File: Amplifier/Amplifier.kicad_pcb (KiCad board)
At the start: 4 copper layers, 94 x 58.4 mm, 47 parts, among them J1 132365-10, J2 SMA-J-P-H-ST-EM1, J3 JST_VH, U1 SKY65111-348LF, U2 MAX2633EUT+T, U3 RLM-23-1WL+, U4 SKYA21001, U5 SKYA21001, U6 TPS63051RMWR

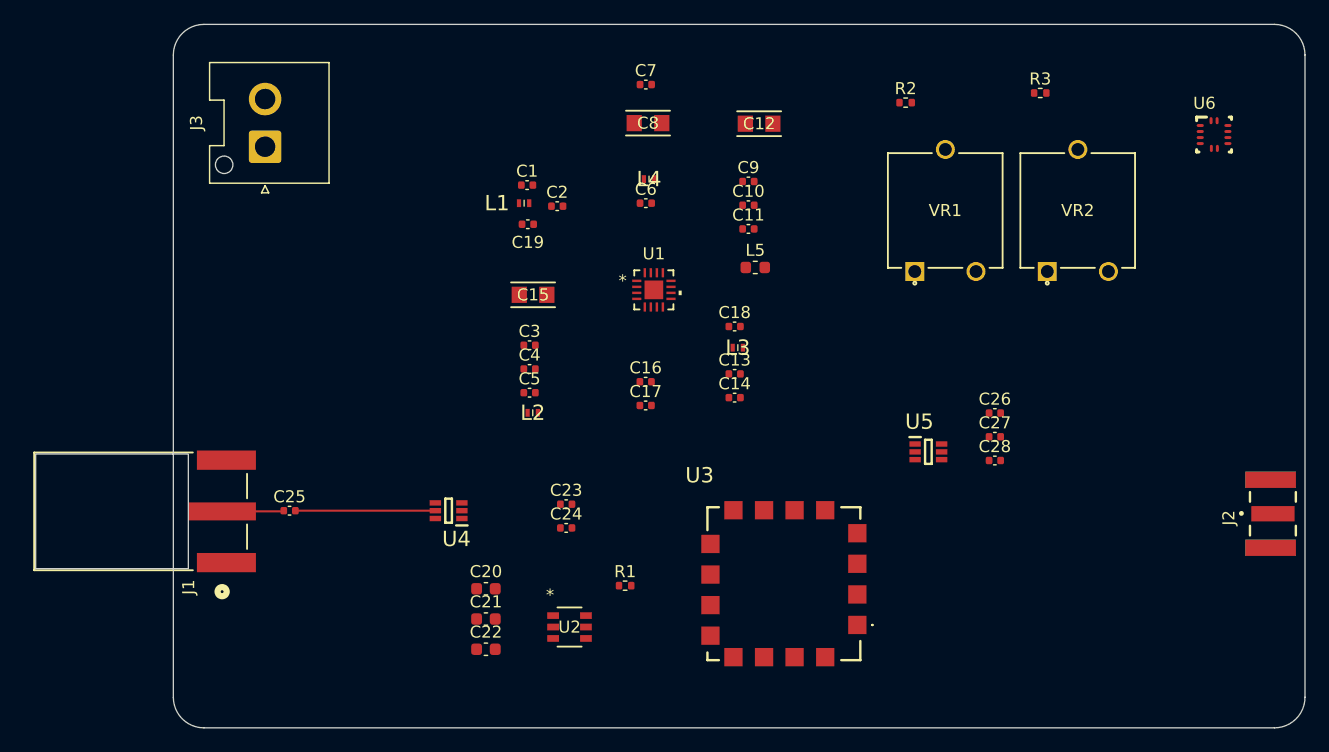
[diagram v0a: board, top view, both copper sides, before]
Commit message: updated component footprint. updated pcb layout.
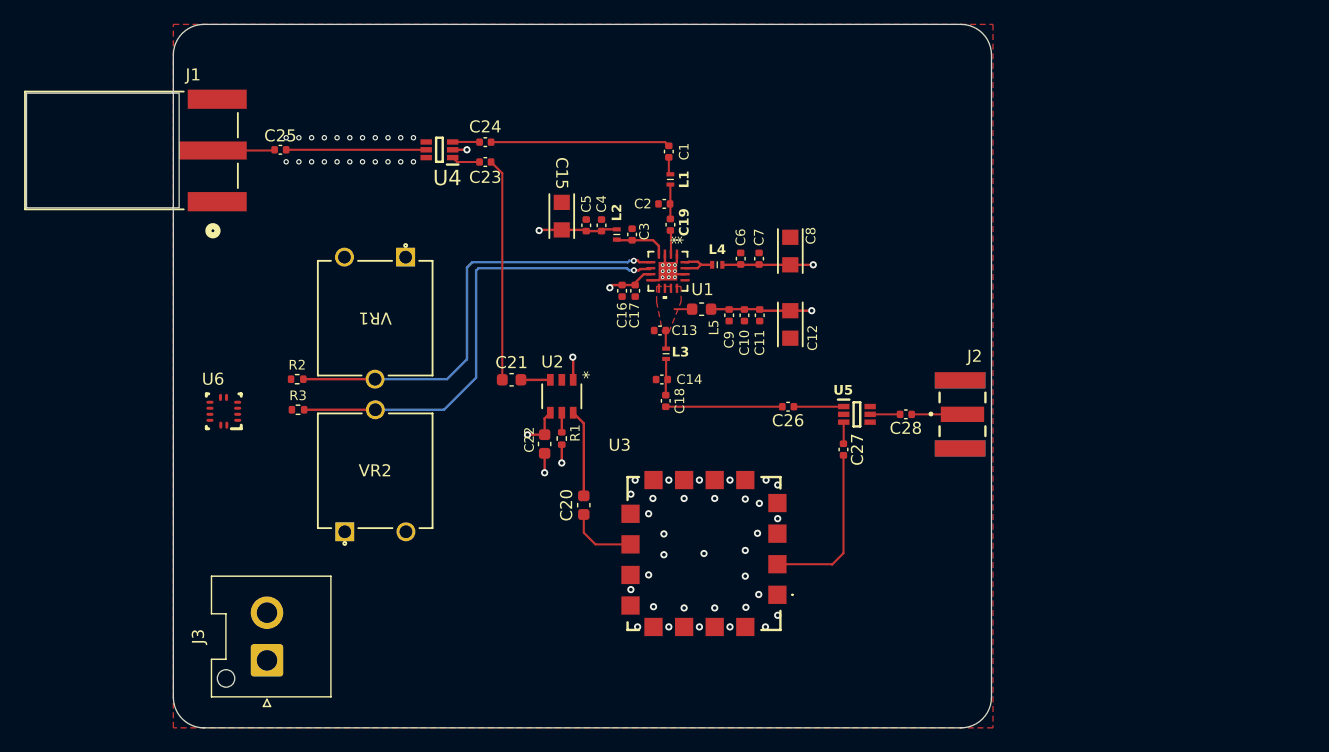
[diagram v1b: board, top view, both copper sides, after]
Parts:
- moved U6 85.4 mm to (88.0, 72.8), turned to 180 degrees
- moved R3 67.0 mm to (94.2, 72.6)
- moved VR2 62.2 mm to (103.1, 72.9)
- moved VR1 55.6 mm to (98.1, 69.8), turned to 180 degrees
- moved R2 55.5 mm to (94.1, 70.1)
- moved J3 42.7 mm to (91.6, 93.5)
- moved C24 32.7 mm to (109.7, 50.4), turned to 180 degrees
- moved J1 30.0 mm to (87.1, 51.1)
- moved C25 30.0 mm to (92.7, 51.1)
- moved U4 30.0 mm to (105.9, 51.1)
- moved C23 29.2 mm to (109.7, 52.1)
- moved J2 27.1 mm to (149.4, 73.0)
- moved C21 20.0 mm to (111.9, 70.2)
- moved U2 19.2 mm to (116.1, 71.5), turned to -90 degrees
- moved C22 17.7 mm to (114.7, 75.5), turned to -90 degrees
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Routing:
- net Vapc2: track 0.00 -> 39.0 mm, vias 0 -> 1
- net Vapc1: track 0.00 -> 37.5 mm, vias 0 -> 1
- net VCC: track 0.00 -> 31.9 mm, vias 0 -> 6
- net LNAout: track 0.00 -> 18.5 mm
- net RFin: track 0.00 -> 14.9 mm
- net INPUT: track 0.00 -> 14.0 mm
- net GND: track 0.00 -> 10.8 mm, vias 0 -> 67
- net RFout: track 0.00 -> 9.68 mm
- net Net-(U2-IN): track 0.00 -> 7.27 mm
- net LIMout: track 0.00 -> 5.79 mm
- net Net-(U1-VCC1): track 0.00 -> 4.39 mm
- net ANT: track 0.00 -> 4.23 mm
- net Net-(U5-J3): track 0.00 -> 4.14 mm
- net Net-(L4-Pad1): track 0.00 -> 3.73 mm
- net Net-(C14-Pad1): track 0.00 -> 3.13 mm
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- added copper zone on F.Cu, net GND
- added copper zone on F.Cu, net Net-(C13-Pad1)
- added copper zone on In2.Cu, net VCC
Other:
- board size 94 x 58.4 mm -> 67.9 x 58.4 mm

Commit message: added/updated caps/inductor for 3v3 reg. updated pcb layout. updated footprints for connectors. started adding fence vias.
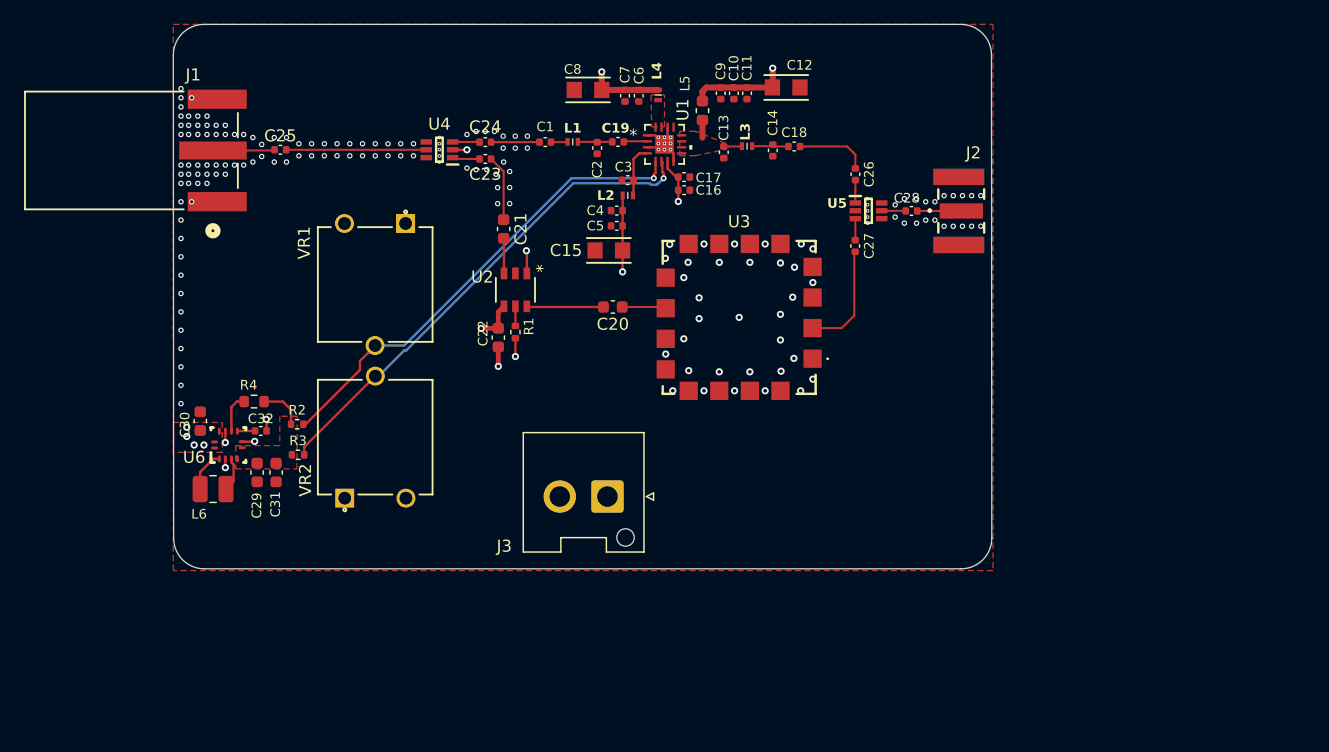
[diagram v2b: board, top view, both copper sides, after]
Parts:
- added C29: 10nF, Capacitor_SMD:C_0603_1608Metric, F.Cu at (90.8, 77.9)
- added C30: 10uF 10V, Capacitor_SMD:C_0603_1608Metric, F.Cu at (86.1, 73.6)
- added C31: 10nF, Capacitor_SMD:C_0603_1608Metric, F.Cu at (92.4, 77.9)
- added C32: 1nF, Capacitor_SMD:C_0402_1005Metric, F.Cu at (91.1, 74.4)
- added L6: 1.5uH, Inductor_SMD:L_1008_2520Metric, F.Cu at (87.1, 79.2)
- added R4: 100k, Resistor_SMD:R_0603_1608Metric, F.Cu at (90.5, 72.0)
- moved J3 31.4 mm to (119.9, 79.9), turned to 180 degrees
- moved C18 23.7 mm to (135.4, 50.8), turned to 0 degrees
- moved C8 21.5 mm to (118.3, 46.1), turned to 180 degrees
- moved C14 21.1 mm to (133.6, 51.1), turned to -90 degrees
- moved C26 20.1 mm to (140.5, 53.1), turned to 90 degrees
- moved U3 19.8 mm to (130.8, 65.0)
- moved C12 19.7 mm to (134.7, 45.9), turned to 0 degrees
- moved L3 18.5 mm to (131.5, 50.8), turned to 0 degrees
- moved C11 18.5 mm to (131.5, 46.4)
- moved C10 18.5 mm to (130.4, 46.4)
- moved C9 18.5 mm to (129.3, 46.4)
- moved C7 17.5 mm to (121.3, 46.6), turned to -90 degrees
- moved C27 16.9 mm to (140.4, 59.0)
- moved U5 16.9 mm to (141.6, 56.1)
- moved C28 16.9 mm to (145.1, 56.1)
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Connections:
- J1 pad 2: (no net) -> GND
- J1 pad 3: (no net) -> GND
- J1 pad 4: (no net) -> GND
- J1 pad 5: (no net) -> GND
- U6 pad 1: unconnected-(U6-L1-Pad1) -> Net-(U6-L1)
- U6 pad 10: unconnected-(U6-ILIM-Pad10) -> VCC
- U6 pad 11: unconnected-(U6-EN-Pad11) -> VCC
- U6 pad 12: unconnected-(U6-VIN-Pad12) -> VCC
- U6 pad 3: unconnected-(U6-L2-Pad3) -> Net-(U6-L2)
- U6 pad 5: unconnected-(U6-FB-Pad5) -> 3v3
- U6 pad 6: unconnected-(U6-PWM-Pad6) -> GND
- U6 pad 7: unconnected-(U6-SS-Pad7) -> Net-(U6-SS)
- U6 pad 8: unconnected-(U6-PG-Pad8) -> Net-(U6-PG)
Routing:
- net LNAout: track 18.5 -> 5.47 mm
- net RFin: track 14.9 -> 4.02 mm
- net INPUT: track 14.0 -> 9.37 mm
- net Net-(L4-Pad1): track 3.73 -> 0.00 mm
- net 3v3: track 0.00 -> 3.73 mm
- net GND: track 10.8 -> 14.5 mm, vias 67 -> 180
- net RFout: track 9.68 -> 6.03 mm
- net Net-(U6-L1): track 0.00 -> 3.46 mm
- net Net-(U6-PG): track 0.00 -> 3.25 mm
- net Net-(U6-L2): track 0.00 -> 2.84 mm
- net LIMout: track 5.79 -> 3.45 mm
- net Vapc2: track 39.0 -> 41.4 mm
- net Net-(U5-J3): track 4.14 -> 1.93 mm
- net VCC: track 31.9 -> 29.7 mm, vias 6 -> 10
- net Vapc1: track 37.5 -> 39.5 mm
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- added copper zone on F.Cu, net 3v3
- added copper zone on F.Cu, net Net-(L4-Pad1)
- added copper zone on F.Cu, net VCC
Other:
- board size 67.9 x 58.4 mm -> 68 x 45.2 mm

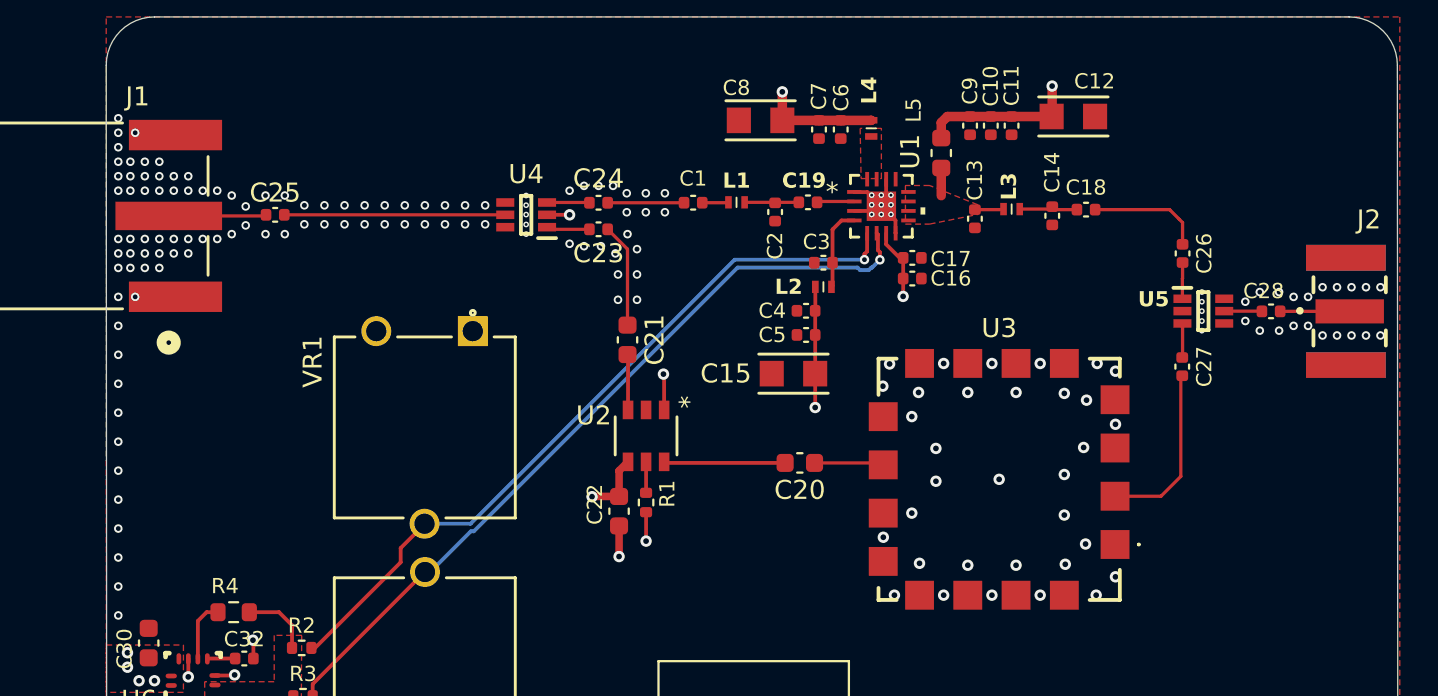
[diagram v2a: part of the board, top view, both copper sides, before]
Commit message: updated note in schematic. updated PCB ground vias/fencing
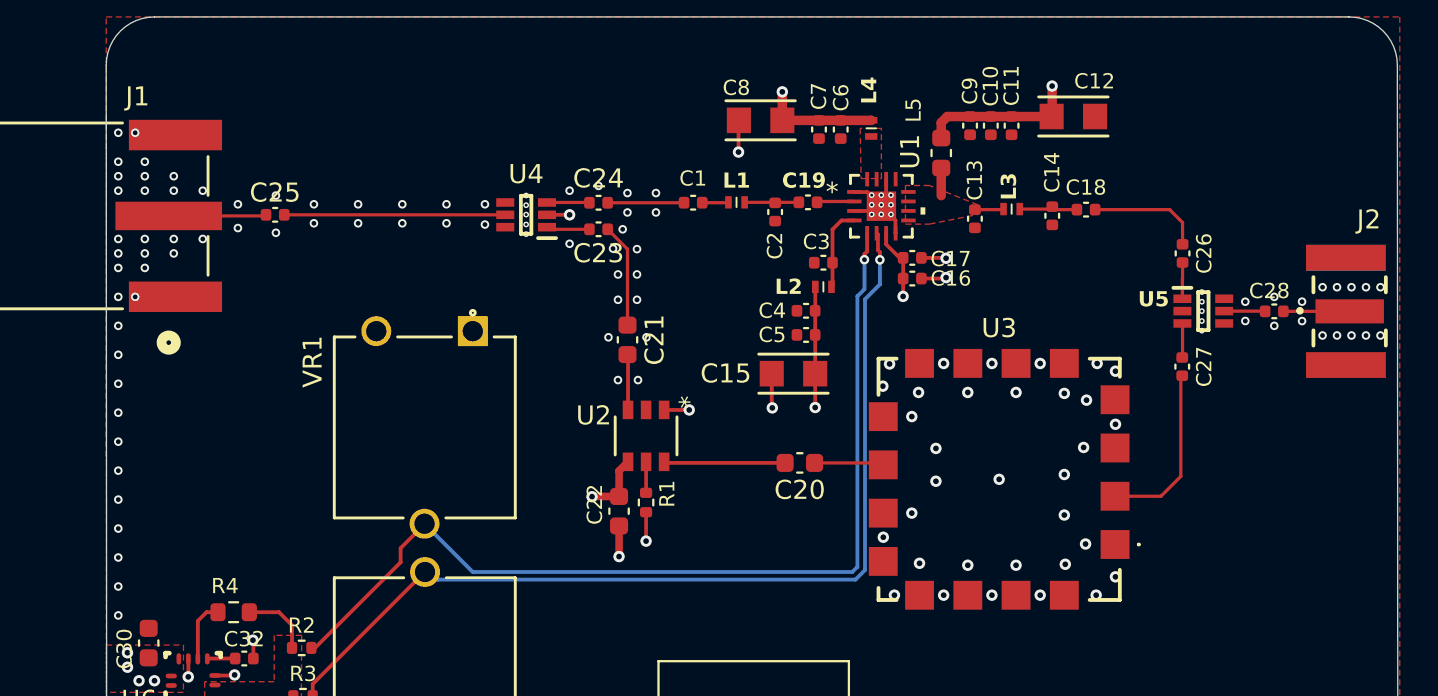
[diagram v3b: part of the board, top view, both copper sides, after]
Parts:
- moved C28 0.17 mm to (145.3, 56.1)
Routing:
- net Vapc1: track 39.5 -> 50.8 mm
- net Vapc2: track 41.4 -> 50.7 mm
- net GND: track 14.5 -> 20.7 mm, vias 180 -> 144
- net VCC: track 29.7 -> 29.2 mm

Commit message: updated via fencing
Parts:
- moved J3 1.08 mm to (120.6, 79.1)
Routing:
- net GND: track 20.7 -> 21.1 mm, vias 144 -> 177
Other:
- board text added: "3V-4.2V IN"
- board text added: "GND"
- board text added: "To Ant"
- board text added: "To T-Beam"
- board text added: "VCC"
